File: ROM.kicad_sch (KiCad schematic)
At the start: 10 parts

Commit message: added decoupling capacitors, perhaps too many? idk better more than less!
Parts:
- added C? (x3): 1U, symbol Device:C_Small
- added C?: (no value), symbol Device:C_Small
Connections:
- net +5V: now also C?.1, C?.1, C?.1, C?.1
- net GND: now also C?.2, C?.2, C?.2, C?.2
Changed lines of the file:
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@@
+    (pin "1")
+  )
+  (symbol (lib_id "power:GNDD") (at 79.375 175.26 0) (unit 1)
+    (in_bom yes) (on_board yes) (fields_autoplaced)
+    (property "Reference" "#PWR?" (id 0) (at 79.375 181.61 0)
+      (effects (font (size 1.27 1.27)) hide)
+    )
+    (property "Value" "GNDD" (id 1) (at 79.375 179.705 0))
+    (property "Footprint" "" (id 2) (at 79.375 175.26 0)
+      (effects (font (size 1.27 1.27)) hide)
+    )
+    (property "Datasheet" "" (id 3) (at 79.375 175.26 0)
+      (effects (font (size 1.27 1.27)) hide)
+    )
     (pin "1")
   )
@@
     )
     (pin "1")
+  )
+  (symbol (lib_id "Device:C_Small") (at 168.275 172.72 0) (unit 1)
+    (in_bom yes) (on_board yes) (fields_autoplaced)
+    (property "Reference" "C?" (id 0) (at 171.45 171.4562 0)
+      (effects (font (size 1.27 1.27)) (justify left))
+    )
+    (property "Value" "1U" (id 1) (at 171.45 173.9962 0)
+      (effects (font (size 1.27 1.27)) (justify left))
+    )
+    (property "Footprint" "" (id 2) (at 168.275 172.72 0)
+      (effects (font (size 1.27 1.27)) hide)
+    )
+    (property "Datasheet" "~" (id 3) (at 168.275 172.72 0)
+      (effects (font (size 1.27 1.27)) hide)
+    )
+    (pin "1")
+    (pin "2")
+  )
+  (symbol (lib_id "Device:C_Small") (at 79.375 96.52 0) (unit 1)
+    (in_bom yes) (on_board yes) (fields_autoplaced)
+    (property "Reference" "C?" (id 0) (at 82.55 95.2562 0)
+      (effects (font (size 1.27 1.27)) (justify left))
+    )
+    (property "Value" "" (id 1) (at 82.55 97.7962 0)
+      (effects (font (size 1.27 1.27)) (justify left))
+    )
+    (property "Footprint" "" (id 2) (at 79.375 96.52 0)
+      (effects (font (size 1.27 1.27)) hide)
+    )
+    (property "Datasheet" "~" (id 3) (at 79.375 96.52 0)
+      (effects (font (size 1.27 1.27)) hide)
+    )
+    (pin "1")
+    (pin "2")
+  )
+  (symbol (lib_id "Device:C_Small") (at 79.375 172.72 0) (unit 1)
+    (in_bom yes) (on_board yes) (fields_autoplaced)
+    (property "Reference" "C?" (id 0) (at 82.55 171.4562 0)
+      (effects (font (size 1.27 1.27)) (justify left))
+    )
+    (property "Value" "1U" (id 1) (at 82.55 173.9962 0)
+      (effects (font (size 1.27 1.27)) (justify left))
+    )
+    (property "Footprint" "" (id 2) (at 79.375 172.72 0)
+      (effects (font (size 1.27 1.27)) hide)
+    )
+    (property "Datasheet" "~" (id 3) (at 79.375 172.72 0)
+      (effects (font (size 1.27 1.27)) hide)
+    )
+    (pin "1")
+    (pin "2")
   )
   (symbol (lib_id "74xGxx:74LVC1G32") (at 248.92 83.82 0) (unit 1)
@@
     (pin "4")
     (pin "5")
+  )
+  (symbol (lib_id "power:GNDD") (at 79.375 99.06 0) (unit 1)
+    (in_bom yes) (on_board yes) (fields_autoplaced)
+    (property "Reference" "#PWR?" (id 0) (at 79.375 105.41 0)
+      (effects (font (size 1.27 1.27)) hide)
+    )
+    (property "Value" "GNDD" (id 1) (at 79.375 103.505 0))
+    (property "Footprint" "" (id 2) (at 79.375 99.06 0)
+      (effects (font (size 1.27 1.27)) hide)
+    )
+    (property "Datasheet" "" (id 3) (at 79.375 99.06 0)
+      (effects (font (size 1.27 1.27)) hide)
+    )
+    (pin "1")
   )
   (symbol (lib_id "74xGxx:74LVC1G32") (at 248.92 121.92 0) (unit 1)
@@
     (pin "1")
   )
+  (symbol (lib_id "power:+5V") (at 168.275 93.98 0) (unit 1)
+    (in_bom yes) (on_board yes) (fields_autoplaced)
+    (property "Reference" "#PWR?" (id 0) (at 168.275 97.79 0)
+      (effects (font (size 1.27 1.27)) hide)
+    )
+    (property "Value" "+5V" (id 1) (at 168.275 88.265 0))
+    (property "Footprint" "" (id 2) (at 168.275 93.98 0)
+      (effects (font (size 1.27 1.27)) hide)
+    )
+    (property "Datasheet" "" (id 3) (at 168.275 93.98 0)
+      (effects (font (size 1.27 1.27)) hide)
+    )
+    (pin "1")
+  )
   (symbol (lib_id "Memory_Flash:SST39SF040") (at 154.94 68.58 0) (unit 1)
     (in_bom yes) (on_board yes)
@@
     (pin "9")
   )
+  (symbol (lib_id "Device:C_Small") (at 168.275 96.52 0) (unit 1)
+    (in_bom yes) (on_board yes) (fields_autoplaced)
+    (property "Reference" "C?" (id 0) (at 171.45 95.2562 0)
+      (effects (font (size 1.27 1.27)) (justify left))
+    )
+    (property "Value" "1U" (id 1) (at 171.45 97.7962 0)
+      (effects (font (size 1.27 1.27)) (justify left))
+    )
+    (property "Footprint" "" (id 2) (at 168.275 96.52 0)
+      (effects (font (size 1.27 1.27)) hide)
+    )
+    (property "Datasheet" "~" (id 3) (at 168.275 96.52 0)
+      (effects (font (size 1.27 1.27)) hide)
+    )
+    (pin "1")
+    (pin "2")
+  )
   (symbol (lib_id "power:GNDD") (at 66.04 175.26 0) (unit 1)
     (in_bom yes) (on_board yes) (fields_autoplaced)
@@
     (pin "1")
   )
+  (symbol (lib_id "power:GNDD") (at 168.275 175.26 0) (unit 1)
+    (in_bom yes) (on_board yes) (fields_autoplaced)
+    (property "Reference" "#PWR?" (id 0) (at 168.275 181.61 0)
+      (effects (font (size 1.27 1.27)) hide)
+    )
+    (property "Value" "GNDD" (id 1) (at 168.275 179.705 0))
+    (property "Footprint" "" (id 2) (at 168.275 175.26 0)
+      (effects (font (size 1.27 1.27)) hide)
+    )
+    (property "Datasheet" "" (id 3) (at 168.275 175.26 0)
+      (effects (font (size 1.27 1.27)) hide)
+    )
+    (pin "1")
+  )
   (symbol (lib_id "power:+5V") (at 154.94 111.76 0) (unit 1)
     (in_bom yes) (on_board yes) (fields_autoplaced)
@@
     (pin "2")
     (pin "3")
+  )
+  (symbol (lib_id "power:+5V") (at 168.275 170.18 0) (unit 1)
+    (in_bom yes) (on_board yes) (fields_autoplaced)
+    (property "Reference" "#PWR?" (id 0) (at 168.275 173.99 0)
+      (effects (font (size 1.27 1.27)) hide)
+    )
+    (property "Value" "+5V" (id 1) (at 168.275 164.465 0))
+    (property "Footprint" "" (id 2) (at 168.275 170.18 0)
+      (effects (font (size 1.27 1.27)) hide)
+    )
+    (property "Datasheet" "" (id 3) (at 168.275 170.18 0)
+      (effects (font (size 1.27 1.27)) hide)
+    )
+    (pin "1")
   )
   (symbol (lib_id "power:GNDD") (at 247.65 46.99 0) (unit 1)
@@
     (pin "9")
   )
+  (symbol (lib_id "power:GNDD") (at 168.275 99.06 0) (unit 1)
+    (in_bom yes) (on_board yes) (fields_autoplaced)
+    (property "Reference" "#PWR?" (id 0) (at 168.275 105.41 0)
+      (effects (font (size 1.27 1.27)) hide)
+    )
+    (property "Value" "GNDD" (id 1) (at 168.275 103.505 0))
+    (property "Footprint" "" (id 2) (at 168.275 99.06 0)
+      (effects (font (size 1.27 1.27)) hide)
+    )
+    (property "Datasheet" "" (id 3) (at 168.275 99.06 0)
+      (effects (font (size 1.27 1.27)) hide)
+    )
+    (pin "1")
+  )
+  (symbol (lib_id "power:+5V") (at 79.375 93.98 0) (unit 1)
+    (in_bom yes) (on_board yes) (fields_autoplaced)
+    (property "Reference" "#PWR?" (id 0) (at 79.375 97.79 0)
+      (effects (font (size 1.27 1.27)) hide)
+    )
+    (property "Value" "+5V" (id 1) (at 79.375 88.265 0))
+    (property "Footprint" "" (id 2) (at 79.375 93.98 0)
+      (effects (font (size 1.27 1.27)) hide)
+    )
+    (property "Datasheet" "" (id 3) (at 79.375 93.98 0)
+      (effects (font (size 1.27 1.27)) hide)
+    )
+    (pin "1")
+  )
   (symbol (lib_id "power:+5V") (at 247.65 36.83 0) (unit 1)
     (in_bom yes) (on_board yes) (fields_autoplaced)
@@
       (effects (font (size 1.27 1.27)) hide)
     )
+    (pin "1")
+  )
+  (symbol (lib_id "power:+5V") (at 79.375 170.18 0) (unit 1)
+    (in_bom yes) (on_board yes) (fields_autoplaced)
+    (property "Reference" "#PWR?" (id 0) (at 79.375 173.99 0)
+      (effects (font (size 1.27 1.27)) hide)
+    )
+    (property "Value" "+5V" (id 1) (at 79.375 164.465 0))
+    (property "Footprint" "" (id 2) (at 79.375 170.18 0)
+      (effects (font (size 1.27 1.27)) hide)
+    )
+    (property "Datasheet" "" (id 3) (at 79.375 170.18 0)
+      (effects (font (size 1.27 1.27)) hide)
+    )

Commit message: more obvious optimizations
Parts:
- removed U? (x4): 74LVC1G32, symbol 74xGxx:74LVC1G32
- removed U?: 74LVC1G139, symbol 74xGxx:74LVC1G139
- added C?: (no value), symbol Device:C_Small
- added U? (x3): 74AHC139, symbol 74xx:74LS139
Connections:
- net +5V: now also C?.1, U?.15 (E), U?.16 (VCC)
- net EAB_{19}: now also U?.3 (A1)
- net EAB_{20}: now also U?.2 (A0)
- net GND: now also C?.2, U?.13 (A1), U?.14 (A0), U?.8 (GND)
- net ~{ROMEN_{0}}: now also U?.4 (O0)
- net ~{ROMEN_{1}}: now also U?.5 (O1)
- net ~{ROMEN_{2}}: now also U?.6 (O2)
- net ~{ROMEN_{3}}: now also U?.7 (O3)
- net ~{ROMEN}: now also U?.1 (E)
- no-connect marks 0 -> 4

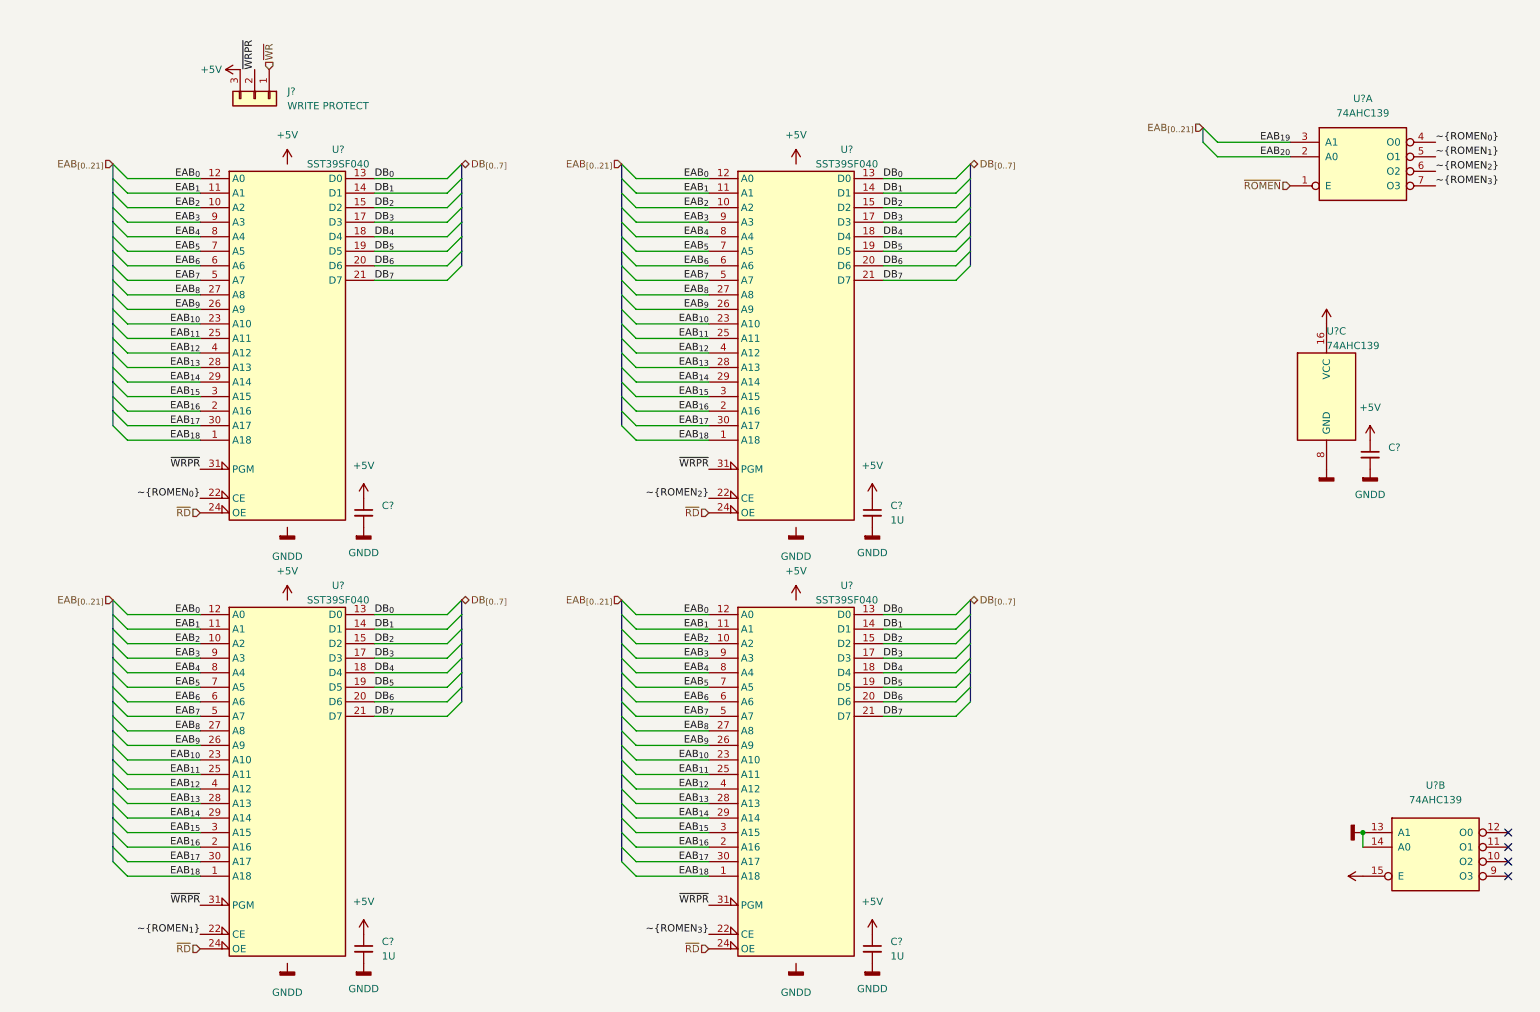
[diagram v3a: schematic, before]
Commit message: some clean up and simplification, as well as some renaming
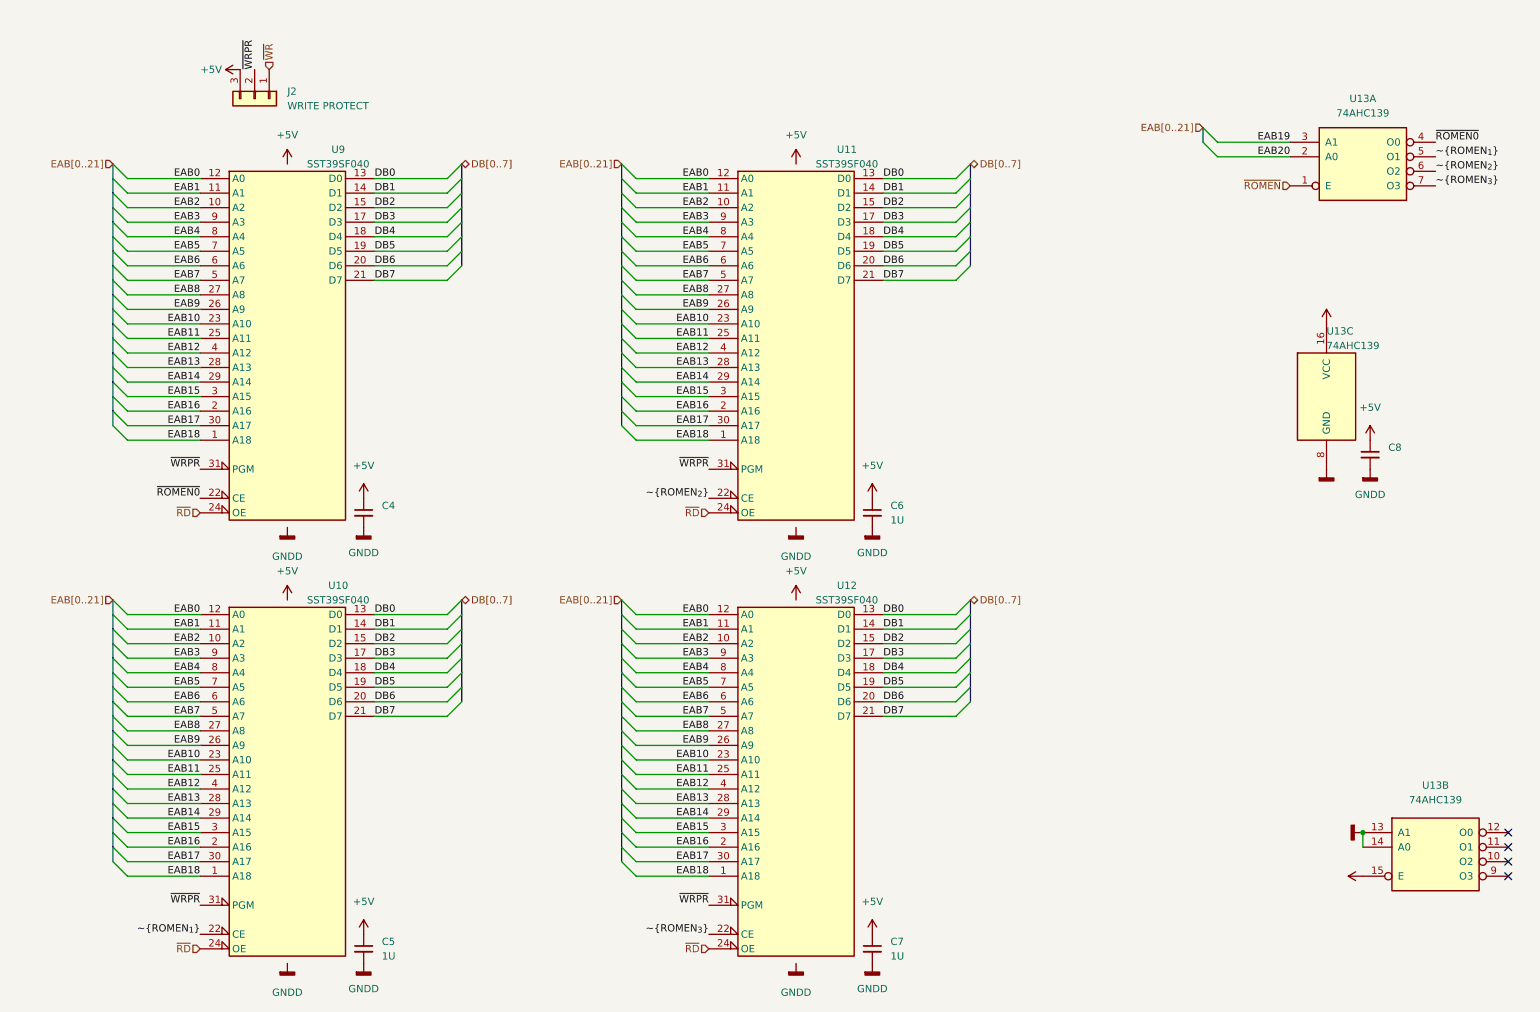
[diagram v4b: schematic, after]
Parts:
- gave numbers to parts that had none: 11
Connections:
- net DB_{0} renamed DB0
- net DB_{1} renamed DB1
- net DB_{2} renamed DB2
- net DB_{3} renamed DB3
- net DB_{4} renamed DB4
- net DB_{5} renamed DB5
- net DB_{6} renamed DB6
- net DB_{7} renamed DB7
- net EAB_{0} renamed EAB0
- net EAB_{10} renamed EAB10
- net EAB_{11} renamed EAB11
- net EAB_{12} renamed EAB12
- net EAB_{13} renamed EAB13
- net EAB_{14} renamed EAB14
- net EAB_{15} renamed EAB15
- net EAB_{16} renamed EAB16
- net EAB_{17} renamed EAB17
- net EAB_{18} renamed EAB18
- net EAB_{19} renamed EAB19
- net EAB_{1} renamed EAB1
- net EAB_{20} renamed EAB20
- net EAB_{2} renamed EAB2
- net EAB_{3} renamed EAB3
- net EAB_{4} renamed EAB4
- net EAB_{5} renamed EAB5
- net EAB_{6} renamed EAB6
- net EAB_{7} renamed EAB7
- net EAB_{8} renamed EAB8
- net EAB_{9} renamed EAB9
- net ~{ROMEN_{0}} renamed ~{ROMEN0}

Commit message: begin integration of logic into atf1508
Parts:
- C4: value (none) -> 1U; footprint (none) -> Capacitor_SMD:C_1206_3216Metric
- C5, C6, C7: footprint (none) -> Capacitor_SMD:C_1206_3216Metric
- C8: value (none) -> 0U1; footprint (none) -> Capacitor_SMD:C_0603_1608Metric
- J2: footprint (none) -> Connector_PinHeader_2.54mm:PinHeader_1x03_P2.54mm_Vertical
- U10, U11, U12, U9: footprint (none) -> Package_SO:TSOP-I-32_14.4x8mm_P0.5mm
- U13: footprint (none) -> Package_SO:TSSOP-16_4.4x5mm_P0.65mm
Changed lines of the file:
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@@
     (property "Reference" "U12" (id 0) (at 163.83 109.22 0))
     (property "Value" "SST39SF040" (id 1) (at 163.83 111.76 0))
-    (property "Footprint" "" (id 2) (at 154.94 137.16 0)
+    (property "Footprint" "Package_SO:TSOP-I-32_14.4x8mm_P0.5mm" (id 2) (at 154.94 137.16 0)
       (effects (font (size 1.27 1.27)) hide)
     )
@@
       (effects (font (size 1.27 1.27)) hide)
     )
-    (property "Value" "" (id 1) (at 247.65 93.98 0))
+    (property "Value" "GNDD" (id 1) (at 247.65 93.98 0))
     (property "Footprint" "" (id 2) (at 247.65 88.9 0)
       (effects (font (size 1.27 1.27)) hide)
@@
       (effects (font (size 1.27 1.27)) hide)
     )
-    (property "Value" "" (id 1) (at 247.65 58.42 0))
+    (property "Value" "+5V" (id 1) (at 247.65 58.42 0))
     (property "Footprint" "" (id 2) (at 247.65 63.5 0)
       (effects (font (size 1.27 1.27)) hide)
@@
       (effects (font (size 1.27 1.27)) hide)
     )
-    (property "Value" "" (id 1) (at 250.19 152.3999 90)
+    (property "Value" "GNDD" (id 1) (at 250.19 152.3999 90)
       (effects (font (size 1.27 1.27)) (justify right))
     )
@@
       (effects (font (size 1.27 1.27)) (justify left))
     )
-    (property "Footprint" "" (id 2) (at 168.275 172.72 0)
+    (property "Footprint" "Capacitor_SMD:C_1206_3216Metric" (id 2) (at 168.275 172.72 0)
       (effects (font (size 1.27 1.27)) hide)
     )
@@
       (effects (font (size 1.27 1.27)) (justify left))
     )
-    (property "Value" "" (id 1) (at 82.55 97.7962 0)
-      (effects (font (size 1.27 1.27)) (justify left))
-    )
-    (property "Footprint" "" (id 2) (at 79.375 96.52 0)
+    (property "Value" "1U" (id 1) (at 82.55 97.7962 0)
+      (effects (font (size 1.27 1.27)) (justify left))
+    )
+    (property "Footprint" "Capacitor_SMD:C_1206_3216Metric" (id 2) (at 79.375 96.52 0)
       (effects (font (size 1.27 1.27)) hide)
     )
@@
       (effects (font (size 1.27 1.27)) (justify left))
     )
-    (property "Footprint" "" (id 2) (at 79.375 172.72 0)
+    (property "Footprint" "Capacitor_SMD:C_1206_3216Metric" (id 2) (at 79.375 172.72 0)
       (effects (font (size 1.27 1.27)) hide)
     )
@@
       (effects (font (size 1.27 1.27)) hide)
     )
-    (property "Value" "" (id 1) (at 250.19 160.0199 90)
+    (property "Value" "+5V" (id 1) (at 250.19 160.0199 90)
       (effects (font (size 1.27 1.27)) (justify left))
     )
@@
     (property "Reference" "U13" (id 0) (at 266.7 144.145 0))
     (property "Value" "74AHC139" (id 1) (at 266.7 146.685 0))
-    (property "Footprint" "" (id 2) (at 266.7 154.94 0)
+    (property "Footprint" "Package_SO:TSSOP-16_4.4x5mm_P0.65mm" (id 2) (at 266.7 154.94 0)
       (effects (font (size 1.27 1.27)) hide)
     )
@@
     (property "Reference" "U13" (id 0) (at 254 24.13 0))
     (property "Value" "74AHC139" (id 1) (at 254 26.67 0))
-    (property "Footprint" "" (id 2) (at 254 34.29 0)
+    (property "Footprint" "Package_SO:TSSOP-16_4.4x5mm_P0.65mm" (id 2) (at 254 34.29 0)
       (effects (font (size 1.27 1.27)) hide)
     )
@@
     (property "Reference" "U9" (id 0) (at 74.93 33.02 0))
     (property "Value" "SST39SF040" (id 1) (at 74.93 35.56 0))
-    (property "Footprint" "" (id 2) (at 66.04 60.96 0)
+    (property "Footprint" "Package_SO:TSOP-I-32_14.4x8mm_P0.5mm" (id 2) (at 66.04 60.96 0)
       (effects (font (size 1.27 1.27)) hide)
     )
@@
       (effects (font (size 1.27 1.27)) (justify left))
     )
-    (property "Footprint" "" (id 2) (at 247.65 76.2 0)
+    (property "Footprint" "Package_SO:TSSOP-16_4.4x5mm_P0.65mm" (id 2) (at 247.65 76.2 0)
       (effects (font (size 1.27 1.27)) hide)
     )
@@
     (property "Reference" "U11" (id 0) (at 163.83 33.02 0))
     (property "Value" "SST39SF040" (id 1) (at 163.83 35.56 0))
-    (property "Footprint" "" (id 2) (at 154.94 60.96 0)
+    (property "Footprint" "Package_SO:TSOP-I-32_14.4x8mm_P0.5mm" (id 2) (at 154.94 60.96 0)
       (effects (font (size 1.27 1.27)) hide)
     )
@@
       (effects (font (size 1.27 1.27)) (justify left))
     )
-    (property "Footprint" "" (id 2) (at 168.275 96.52 0)
+    (property "Footprint" "Capacitor_SMD:C_1206_3216Metric" (id 2) (at 168.275 96.52 0)
       (effects (font (size 1.27 1.27)) hide)
     )
@@
       (effects (font (size 1.27 1.27)) (justify left))
     )
-    (property "Footprint" "" (id 2) (at 60.325 24.13 0)
+    (property "Footprint" "Connector_PinHeader_2.54mm:PinHeader_1x03_P2.54mm_Vertical" (id 2) (at 60.325 24.13 0)
       (effects (font (size 1.27 1.27)) hide)
     )
@@
     (property "Reference" "U10" (id 0) (at 74.93 109.22 0))
     (property "Value" "SST39SF040" (id 1) (at 74.93 111.76 0))
-    (property "Footprint" "" (id 2) (at 66.04 137.16 0)
+    (property "Footprint" "Package_SO:TSOP-I-32_14.4x8mm_P0.5mm" (id 2) (at 66.04 137.16 0)
       (effects (font (size 1.27 1.27)) hide)
     )
@@
       (effects (font (size 1.27 1.27)) (justify left))
     )
-    (property "Value" "" (id 1) (at 258.445 87.6362 0)
-      (effects (font (size 1.27 1.27)) (justify left))
-    )
-    (property "Footprint" "" (id 2) (at 255.27 86.36 0)
-      (effects (font (size 1.27 1.27)) hide)
-    )
+    (property "Value" "0U1" (id 1) (at 258.445 87.6362 0)
+      (effects (font (size 1.27 1.27)) (justify left))
+    )
+    (property "Footprint" "Capacitor_SMD:C_0603_1608Metric" (id 2) (at 255.27 86.36 0)
+      (effects (font (size 1.27 1.27)) hide)
+    )
